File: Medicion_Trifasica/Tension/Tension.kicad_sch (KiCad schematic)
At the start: 9 parts, among them J1 Vo, U1 LM358

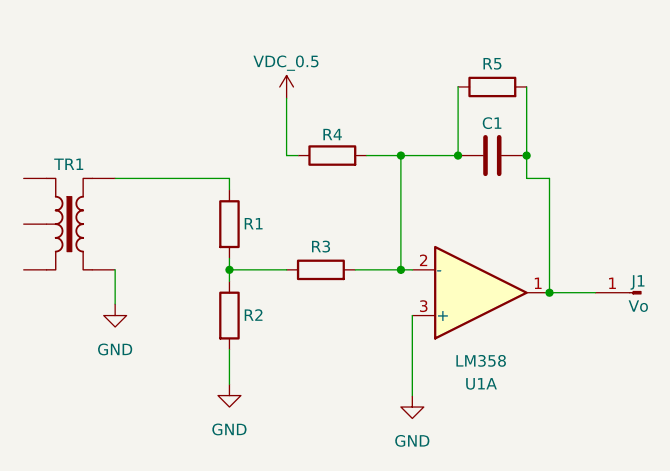
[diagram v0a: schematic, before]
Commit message: Se agregaron valores a la medicion de tension
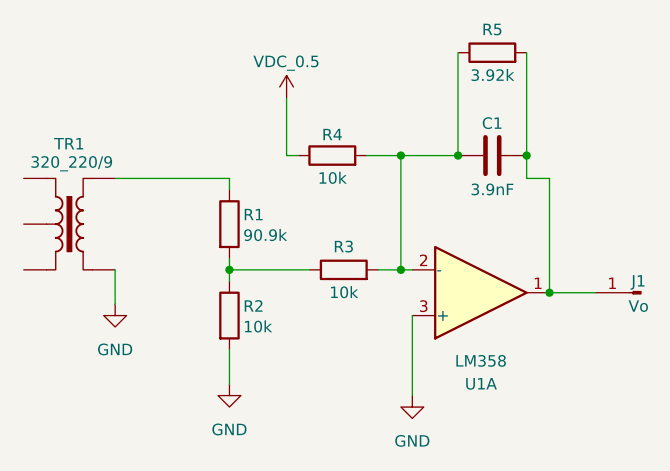
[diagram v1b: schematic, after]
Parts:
- C1: value C -> 3.9nF
- R1: value R -> 90.9k
- R2, R3, R4: value R -> 10k
- R5: value R -> 3.92k
- TR1: value TRANSF4 -> 320_220/9
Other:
- moved on the sheet: R3, R5
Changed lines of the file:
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@@
 	(wire
 		(pts
-			(xy 76.2 66.04) (xy 81.28 66.04)
-		)
-		(stroke
-			(width 0)
-			(type default)
-		)
-	)
-	(wire
-		(pts
-			(xy 62.23 66.04) (xy 68.58 66.04)
-		)
-		(stroke
-			(width 0)
-			(type default)
-		)
-	)
-	(wire
-		(pts
-			(xy 95.25 45.72) (xy 95.25 53.34)
+			(xy 78.74 66.04) (xy 81.28 66.04)
+		)
+		(stroke
+			(width 0)
+			(type default)
+		)
+	)
+	(wire
+		(pts
+			(xy 62.23 66.04) (xy 71.12 66.04)
+		)
+		(stroke
+			(width 0)
+			(type default)
+		)
+	)
+	(wire
+		(pts
+			(xy 95.25 41.91) (xy 95.25 53.34)
 		)
 		(stroke
@@
 	(wire
 		(pts
-			(xy 87.63 45.72) (xy 87.63 53.34)
+			(xy 87.63 41.91) (xy 87.63 53.34)
 		)
 		(stroke
@@
 			)
 		)
-		(property "Value" "C"
-			(at 91.694 49.53 90)
-			(effects
-				(font
-					(size 1.27 1.27)
-				)
-				(hide yes)
+		(property "Value" "3.9nF"
+			(at 91.44 57.15 90)
+			(effects
+				(font
+					(size 1.27 1.27)
+				)
 			)
 		)
@@
 			)
 		)
-		(property "Value" "R"
-			(at 73.66 49.53 90)
-			(effects
-				(font
-					(size 1.27 1.27)
-				)
-				(hide yes)
+		(property "Value" "10k"
+			(at 73.66 55.88 90)
+			(effects
+				(font
+					(size 1.27 1.27)
+				)
 			)
 		)
@@
 		(dnp no)
 		(property "Reference" "TR1"
-			(at 44.45 54.356 0)
-			(effects
-				(font
-					(size 1.27 1.27)
-				)
-			)
-		)
-		(property "Value" "TRANSF4"
-			(at 44.45 53.34 0)
-			(effects
-				(font
-					(size 1.27 1.27)
-				)
-				(hide yes)
+			(at 44.45 52.07 0)
+			(effects
+				(font
+					(size 1.27 1.27)
+				)
+			)
+		)
+		(property "Value" "320_220/9"
+			(at 44.704 54.102 0)
+			(effects
+				(font
+					(size 1.27 1.27)
+				)
 			)
 		)
@@
 		(dnp no)
 		(property "Reference" "R1"
-			(at 63.754 60.96 0)
+			(at 63.754 59.944 0)
 			(effects
 				(font
@@
 			)
 		)
-		(property "Value" "R"
-			(at 64.77 62.2299 0)
+		(property "Value" "90.9k"
+			(at 63.754 62.23 0)
 			(effects
 				(font
@@
 				)
 				(justify left)
-				(hide yes)
 			)
 		)
@@
 	(symbol
 		(lib_id "Device:R")
-		(at 72.39 66.04 90)
+		(at 74.93 66.04 90)
 		(unit 1)
 		(exclude_from_sim no)
@@
 		(dnp no)
 		(property "Reference" "R3"
-			(at 72.39 63.5 90)
-			(effects
-				(font
-					(size 1.27 1.27)
-				)
-			)
-		)
-		(property "Value" "R"
-			(at 72.39 62.23 90)
-			(effects
-				(font
-					(size 1.27 1.27)
-				)
-				(hide yes)
-			)
-		)
-		(property "Footprint" ""
-			(at 72.39 67.818 90)
+			(at 74.93 63.5 90)
+			(effects
+				(font
+					(size 1.27 1.27)
+				)
+			)
+		)
+		(property "Value" "10k"
+			(at 74.93 68.58 90)
+			(effects
+				(font
+					(size 1.27 1.27)
+				)
+			)
+		)
+		(property "Footprint" ""
+			(at 74.93 67.818 90)
 			(effects
 				(font
@@
 		)
 		(property "Datasheet" "~"
-			(at 72.39 66.04 0)
+			(at 74.93 66.04 0)
 			(effects
 				(font
@@
 		)
 		(property "Description" "Resistor"
-			(at 72.39 66.04 0)
+			(at 74.93 66.04 0)
 			(effects
 				(font
@@
 		(dnp no)
 		(property "Reference" "R2"
-			(at 63.754 71.12 0)
+			(at 63.754 70.104 0)
 			(effects
 				(font
@@
 			)
 		)
-		(property "Value" "R"
-			(at 64.77 72.3899 0)
+		(property "Value" "10k"
+			(at 63.754 72.39 0)
 			(effects
 				(font
@@
 				)
 				(justify left)
-				(hide yes)
 			)
 		)
@@
 	(symbol
 		(lib_id "Device:R")
-		(at 91.44 45.72 90)
+		(at 91.44 41.91 90)
 		(unit 1)
 		(exclude_from_sim no)
@@
 		(dnp no)
 		(property "Reference" "R5"
-			(at 91.44 43.18 90)
-			(effects
-				(font
-					(size 1.27 1.27)
-				)
-			)
-		)
-		(property "Value" "R"
-			(at 91.44 41.91 90)
-			(effects
-				(font
-					(size 1.27 1.27)
-				)
-				(hide yes)
-			)
-		)
-		(property "Footprint" ""
-			(at 91.44 47.498 90)
+			(at 91.44 39.37 90)
+			(effects
+				(font
+					(size 1.27 1.27)
+				)
+			)
+		)
+		(property "Value" "3.92k"
+			(at 91.44 44.45 90)
+			(effects
+				(font
+					(size 1.27 1.27)
+				)
+			)
+		)
+		(property "Footprint" ""
+			(at 91.44 43.688 90)
 			(effects
 				(font
@@
 		)
 		(property "Datasheet" "~"
-			(at 91.44 45.72 0)
+			(at 91.44 41.91 0)
 			(effects
 				(font
@@
 		)
 		(property "Description" "Resistor"
-			(at 91.44 45.72 0)
-			(effects
-				(font
+			(at 91.44 41.91 0)
+			(effects
+				(font

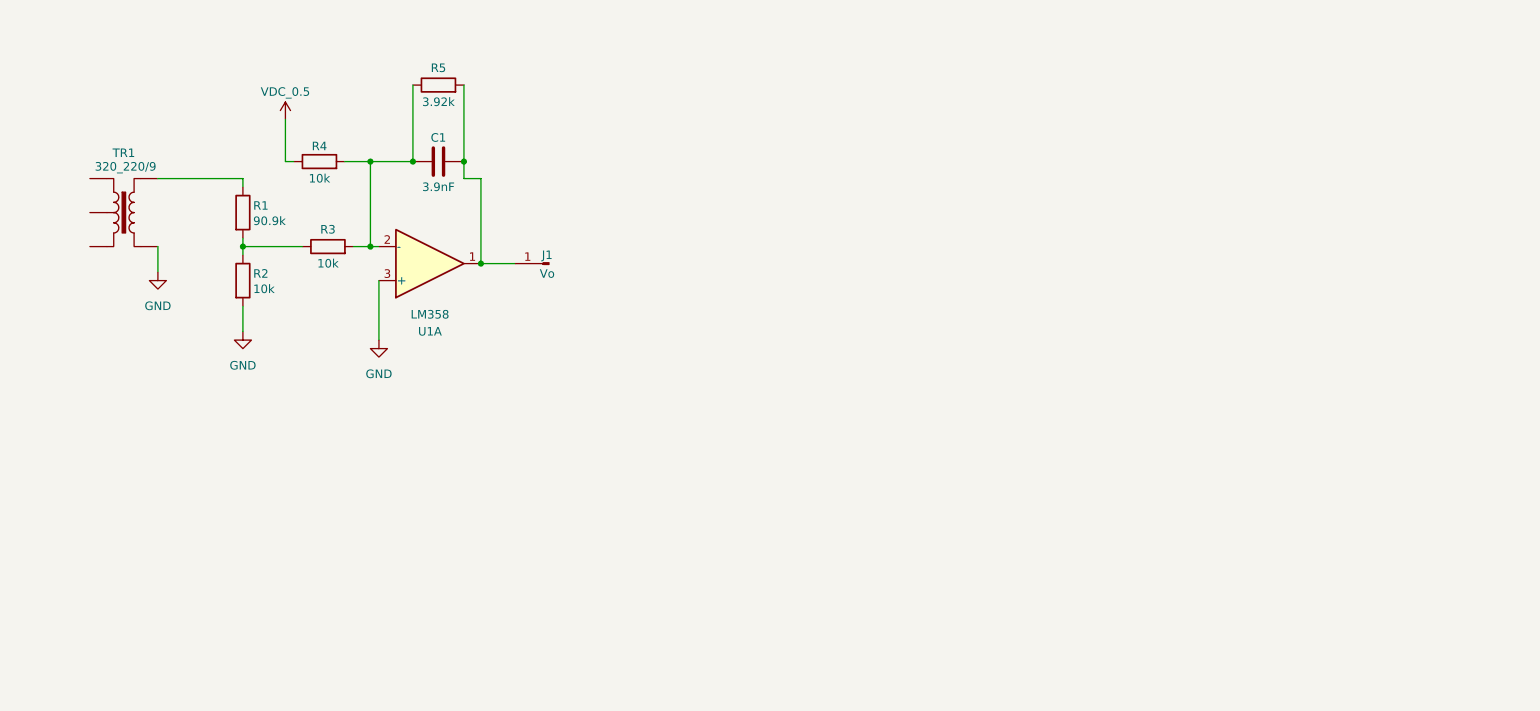
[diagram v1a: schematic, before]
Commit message: Modificaciones finales a los circuitos de medicion de corriente y tension
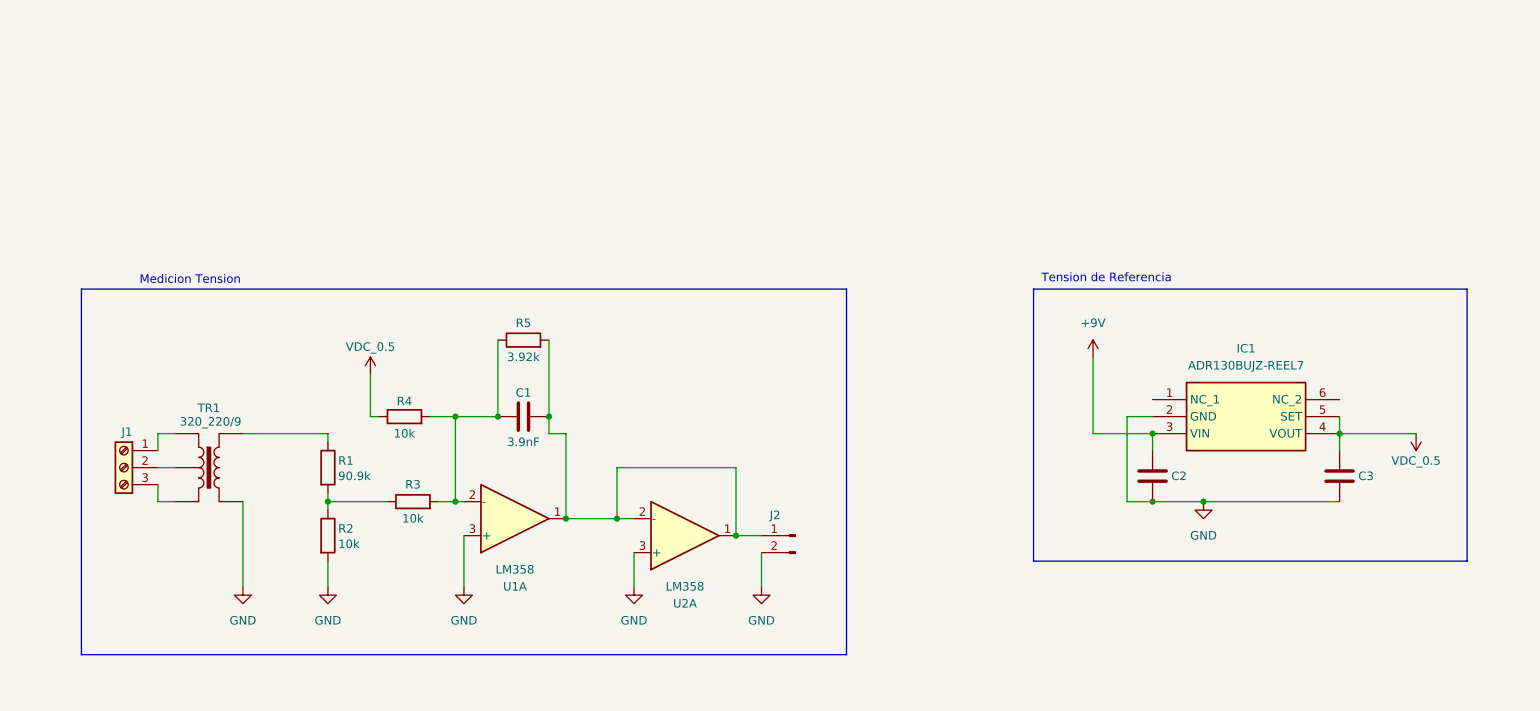
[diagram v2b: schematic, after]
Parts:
- removed J1: Vo, symbol Connector:Conn_01x01_Pin
- added C2, C3: C, symbol Device:C
- added IC1: ADR130BUJZ-REEL7, SOT95P280X100-6N, symbol ADR130BUJZ-REEL7:ADR130BUJZ-REEL7
- added J1: Screw_Terminal_01x03, symbol Connector:Screw_Terminal_01x03
- added J2: Conn_01x02_Pin, symbol Connector:Conn_01x02_Pin
- added U2: LM358, symbol Amplifier_Operational:LM358
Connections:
- net GND: now also C2.2, C3.2, IC1.2 (GND), J2.2 (Pin_2), U2.3 (+)
- net VDC_0.5: now also C3.1, IC1.4 (VOUT), IC1.5 (SET)
- net at C1.2, R5.2, U1.1: now also J2.1 (Pin_1), U2.1, U2.2 (-)
- net at TR1.1: now also J1.1 (Pin_1)
- net at TR1.2: now also J1.2 (Pin_2)
- net at TR1.3: now also J1.3 (Pin_3)
- new net +9V: C2.1, IC1.3 (VIN)
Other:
- note added: "Medicion Tension"
- note added: "Tension de Referencia"
- company: (none) -> U.N.R
- title: (none) -> Medicion de Tension
- moved on the sheet: C1, R1, R2, R3, R4, R5, TR1, U1A

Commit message: Update Tension.kicad_sch
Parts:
- C1: value 3.9nF -> 1.5nF
- R3: value 10k -> 20k
- R5: value 3.92k -> 10k
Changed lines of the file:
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@@
 			)
 		)
-		(property "Value" "3.9nF"
+		(property "Value" "1.5nF"
 			(at 104.14 95.25 90)
 			(effects
@@
 			)
 		)
-		(property "Value" "10k"
+		(property "Value" "20k"
 			(at 87.63 106.68 90)
 			(effects
@@
 			)
 		)
-		(property "Value" "3.92k"
+		(property "Value" "10k"
 			(at 104.14 82.55 90)
 			(effects

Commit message: Se crearon los esquematicos de los circuitos, y sus footprints
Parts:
- removed J1: Screw_Terminal_01x03, symbol Connector:Screw_Terminal_01x03
- removed TR1: 320_220/9, symbol Transformer:TRANSF4
- added J1: Screw_Terminal_01x02, TerminalBlock:TerminalBlock_bornier-2_P5.08mm, symbol Connector:Screw_Terminal_01x02
- added J3: Conn_01x02_Pin, Connector_PinHeader_2.54mm:PinHeader_1x02_P2.54mm_Vertical, symbol Connector:Conn_01x02_Pin
- added T1: Transformer_220/9, Transformer_THT:Transformer_NF_ETAL_1-1_P1200, symbol Device:Transformer_1P_1S
- added unit 3 of U1
- C1: footprint (none) -> Capacitor_SMD:C_0402_1005Metric_Pad0.74x0.62mm_HandSolder
- C2: value C -> 0.1uF; footprint (none) -> Capacitor_SMD:C_0402_1005Metric_Pad0.74x0.62mm_HandSolder
- C3: value C -> 0.1uf; footprint (none) -> Capacitor_SMD:C_0402_1005Metric_Pad0.74x0.62mm_HandSolder
- IC1: footprint SOT95P280X100-6N -> SamacSys_Parts:SOT95P280X100-6N
- J2: footprint (none) -> Connector_PinHeader_2.54mm:PinHeader_1x02_P2.54mm_Horizontal
- R1, R2, R3, R4, R5: footprint (none) -> Resistor_SMD:R_0805_2012Metric_Pad1.20x1.40mm_HandSolder
- U1: renamed from U2; footprint (none) -> Package_SO:SOIC-8_3.9x4.9mm_P1.27mm
- U1: footprint (none) -> Package_SO:SOIC-8_3.9x4.9mm_P1.27mm
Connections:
- net GND: now also U1.5 (+), T1.3 (SA); no longer U1.3 (+)
- net at C1.2, J2.1 (Pin_1), R5.2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: now also U1.6 (-), U1.7; no longer U1.1, U1.2 (-)
- net at R1.1: now also T1.1 (SB)
- new net: J3.2 (Pin_2), U1.4 (V-)
- new net: J3.1 (Pin_1), U1.8 (V+)
- new net: J1.1 (Pin_1), T1.4 (AB)
- new net: J1.2 (Pin_2), T1.6 (AA)

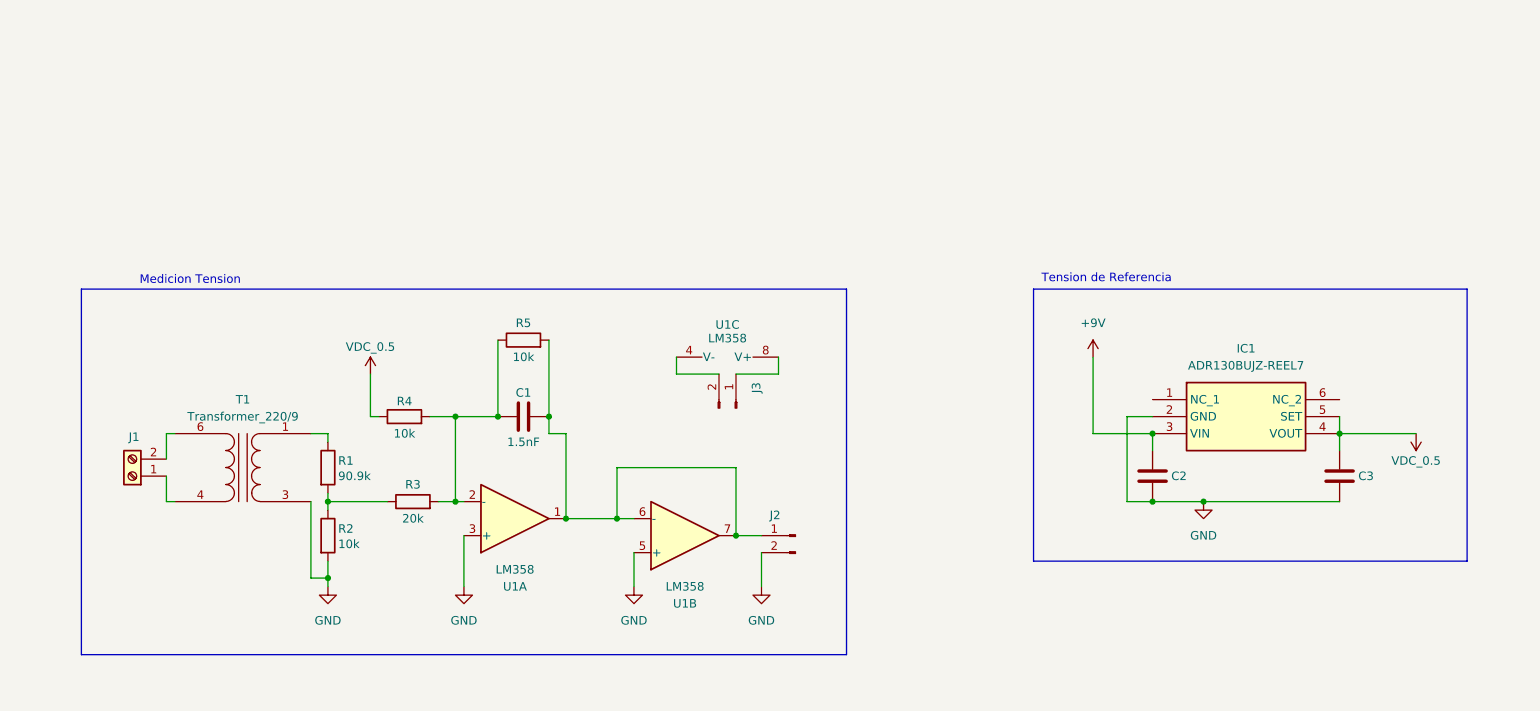
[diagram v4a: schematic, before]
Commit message: Correciones PCBs
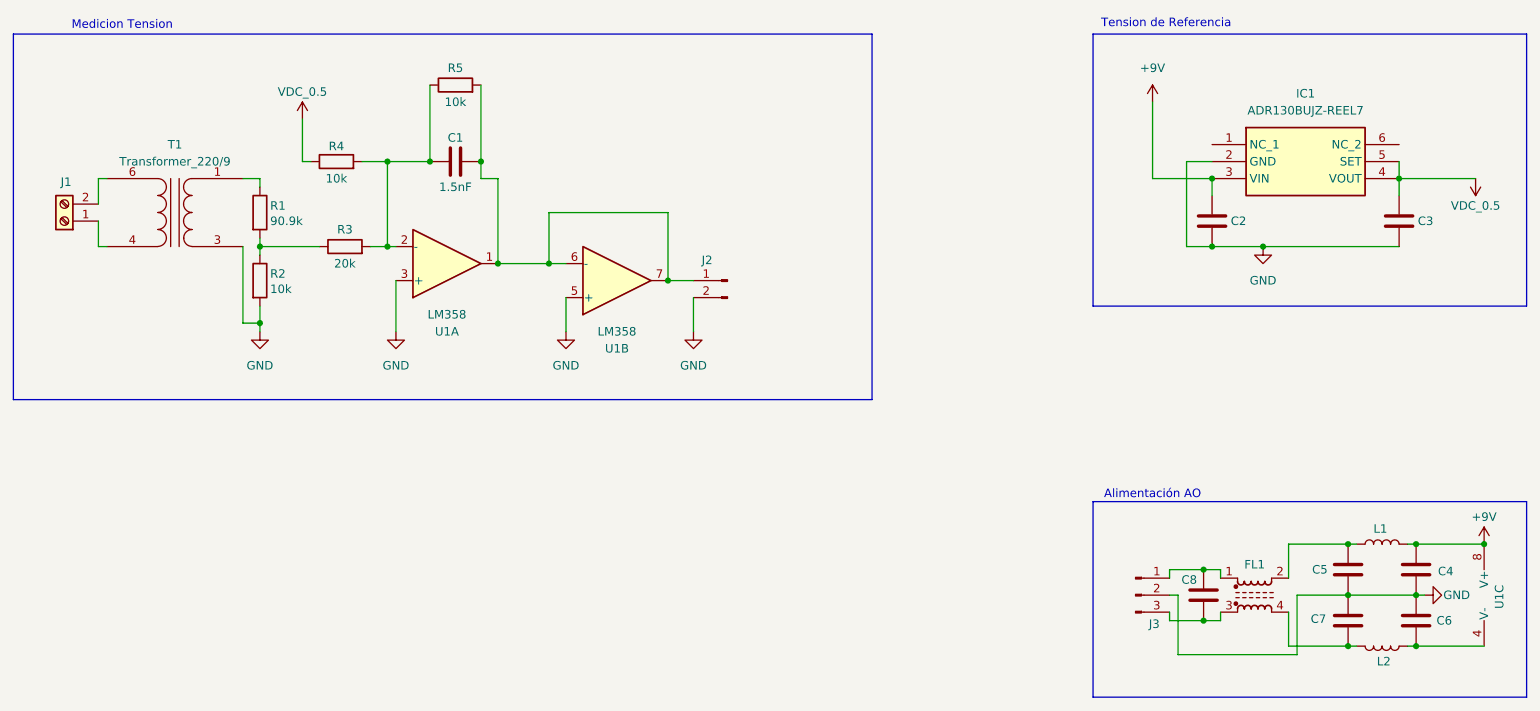
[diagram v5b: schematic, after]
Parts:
- removed J3: Conn_01x02_Pin, Connector_PinHeader_2.54mm:PinHeader_1x02_P2.54mm_Vertical, symbol Connector:Conn_01x02_Pin
- added C4, C5, C6, C7: 100 nF, Capacitor_SMD:C_0402_1005Metric_Pad0.74x0.62mm_HandSolder, symbol Device:C
- added C8: 470 uF, Capacitor_SMD:C_0402_1005Metric_Pad0.74x0.62mm_HandSolder, symbol Device:C
- added FL1: Choke_CommonMode_FerriteCore_1234, Inductor_THT:Choke_EPCOS_B82722A, symbol Filter:Choke_CommonMode_FerriteCore_1234
- added J3: Conn_01x03_Pin, Connector_PinHeader_2.54mm:PinHeader_1x03_P2.54mm_Vertical, symbol Connector:Conn_01x03_Pin
- added L1, L2: 30 uH, Inductor_SMD:L_7.3x7.3_H3.5, symbol Device:L
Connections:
- net +9V: now also U1.8 (V+), C4.2, L1.2
- net GND: now also C4.1, C5.1, C6.1, C7.1, J3.2 (Pin_2)
- net at U1.4 (V-): now also C6.2, L2.1
- new net: C7.2, FL1.4, L2.2
- new net: C8.1, FL1.1, J3.1 (Pin_1)
- new net: C8.2, FL1.3, J3.3 (Pin_3)
- new net: C5.2, FL1.2, L1.1
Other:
- note added: "Alimentación AO"
- moved on the sheet: C1, C2, C3, IC1, J1, J2, R1, R2, R3, R4, R5, T1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

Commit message: Mejora en la organizacion de los circuitos con netclases y colores
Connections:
- net AO_SUM_e+: now reaches C1.1, R3.2, R4.2, R5.1, U1.2 (-)
- net Voltage_O_Buffer: now reaches C1.2, J2.1 (Pin_1), R5.2, U1.1, U1.6 (-), U1.7
- net -9V: now reaches C6.2, L2.1, U1.4 (V-)
- net AC-: now reaches J1.1 (Pin_1), T1.4 (AB)
- net AC+: now reaches J1.2 (Pin_2), T1.6 (AA)
- net Input_+9V: now reaches C8.1, FL1.1, J3.1 (Pin_1)
- net Input_-9V: now reaches C8.2, FL1.3, J3.3 (Pin_3)
- net Voltage_Div: now reaches R1.2, R2.1, R3.1
- no-connect marks 0 -> 2
